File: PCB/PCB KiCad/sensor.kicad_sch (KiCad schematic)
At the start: 15 parts

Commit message: first check + add connectors
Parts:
- removed C? (x2): 100n, symbol Device:C
- removed R?: 100, symbol Device:R
- removed R?: 1k, symbol Device:R
- added C?: 100p, symbol Device:C
- added C?: 47n, symbol Device:C
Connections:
- net AIN+: now also C?.1, C?.2
- net AIN-: now also C?.1, C?.2
- net at R?.1: now also C?.2, R?.2, U?.1
- net at R?.1: now also C?.2, R?.1, U?.7
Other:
- moved on the sheet: R?

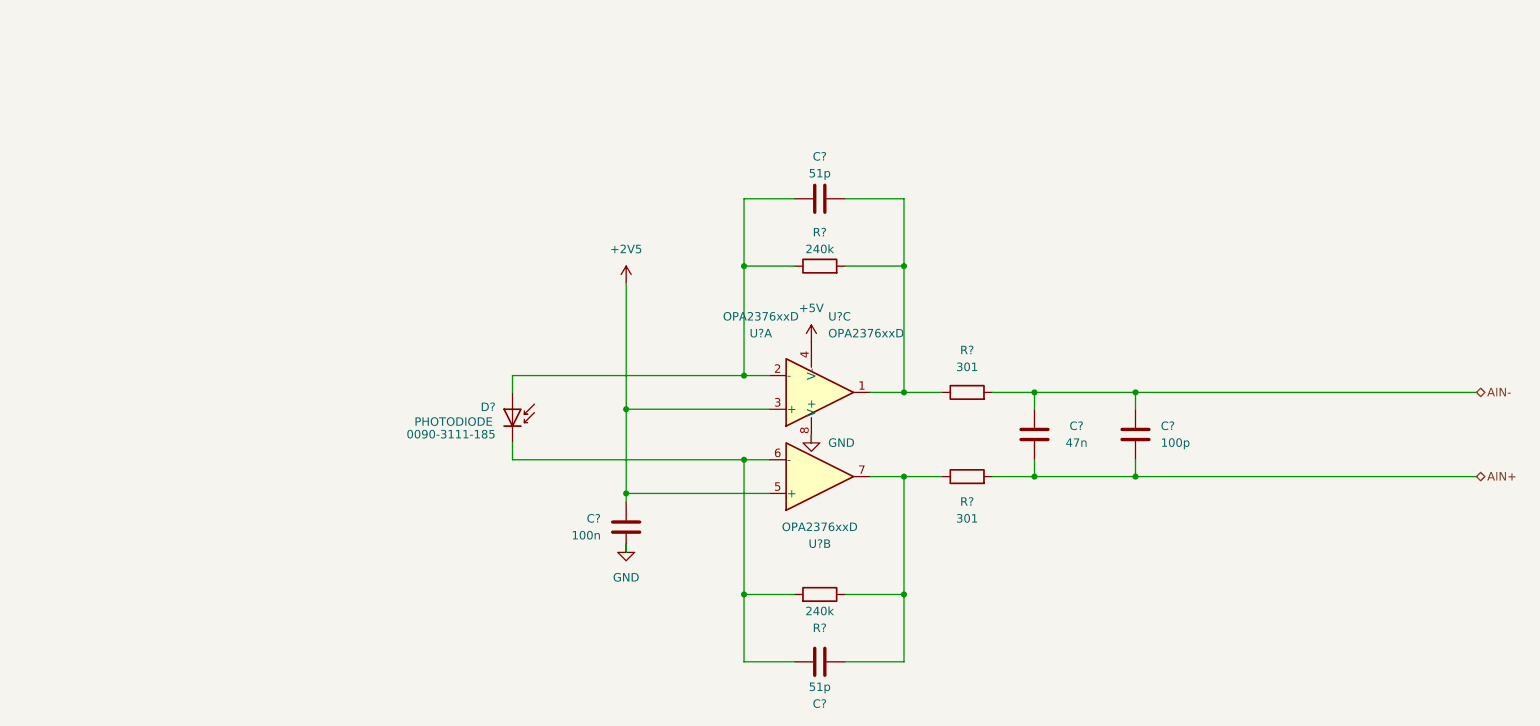
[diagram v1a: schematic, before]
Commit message: ERC: add power flags to satisfy the ERC crap
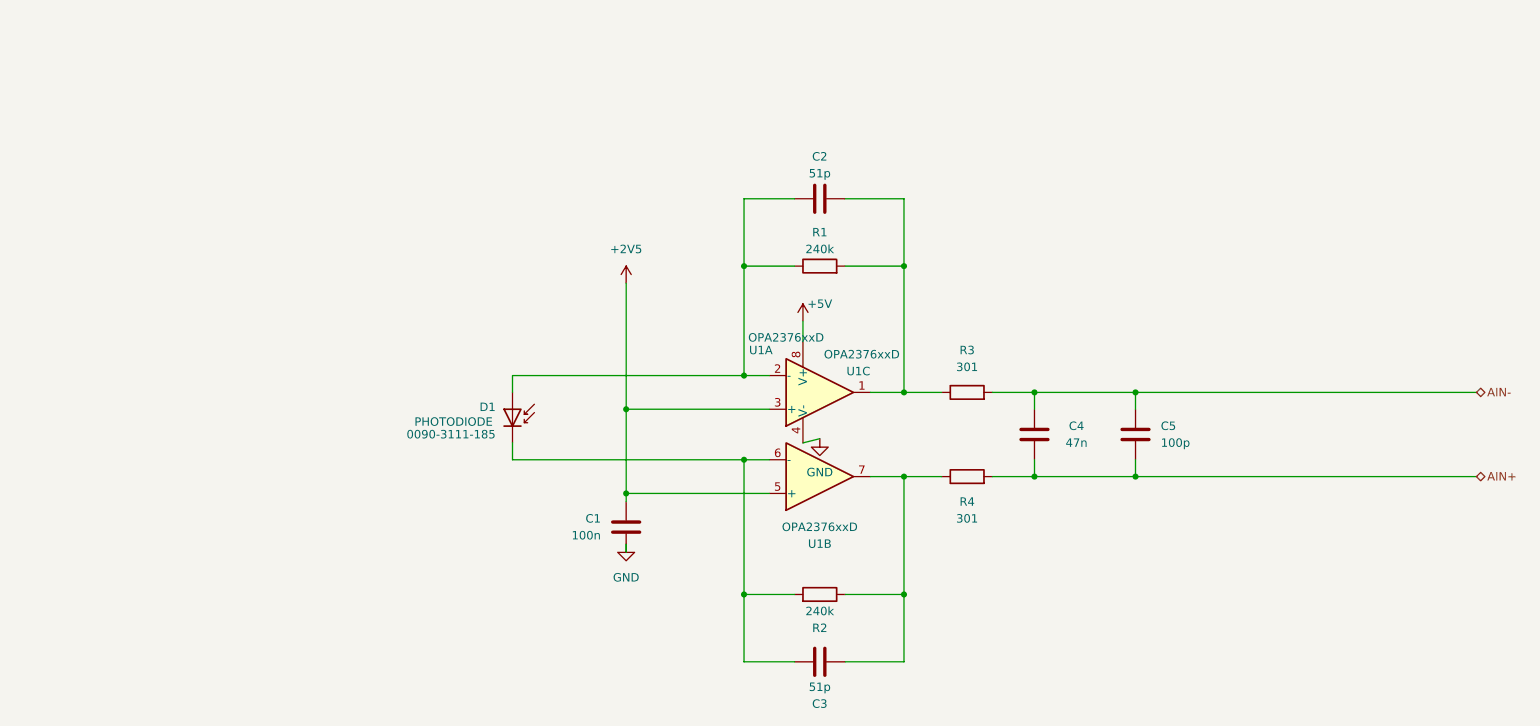
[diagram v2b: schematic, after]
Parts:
- gave numbers to parts that had none: 11
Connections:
- net +5V: now also U1.8 (V+); no longer U1.4 (V-)
- net GND: now also U1.4 (V-); no longer U1.8 (V+)
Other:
- moved on the sheet: U1C
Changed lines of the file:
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@@
     (stroke (width 0) (type default) (color 0 0 0 0))
   )
-  (wire (pts (xy 130.175 99.06) (xy 130.175 100.33))
+  (wire (pts (xy 128.905 100.33) (xy 131.445 99.695))
+    (stroke (width 0) (type default) (color 0 0 0 0))
+  )
+  (wire (pts (xy 128.905 81.915) (xy 128.905 85.09))
     (stroke (width 0) (type default) (color 0 0 0 0))
   )
@@
   (symbol (lib_id "power:GND") (at 102.235 115.57 0) (unit 1)
     (in_bom yes) (on_board yes) (fields_autoplaced)
-    (property "Reference" "#PWR?" (id 0) (at 102.235 121.92 0)
+    (property "Reference" "#PWR02" (id 0) (at 102.235 121.92 0)
       (effects (font (size 1.27 1.27)) hide)
     )
@@
   (symbol (lib_id "Device:R") (at 131.445 123.19 270) (mirror x) (unit 1)
     (in_bom yes) (on_board yes)
-    (property "Reference" "R?" (id 0) (at 131.445 128.27 90))
+    (property "Reference" "R2" (id 0) (at 131.445 128.27 90))
     (property "Value" "240k" (id 1) (at 131.445 125.73 90))
     (property "Footprint" "" (id 2) (at 131.445 124.968 90)
@@
   (symbol (lib_id "Device:R") (at 153.67 92.71 90) (unit 1)
     (in_bom yes) (on_board yes)
-    (property "Reference" "R?" (id 0) (at 153.67 86.36 90))
+    (property "Reference" "R3" (id 0) (at 153.67 86.36 90))
     (property "Value" "301" (id 1) (at 153.67 88.9 90))
     (property "Footprint" "" (id 2) (at 153.67 94.488 90)
@@
   (symbol (lib_id "Device:R") (at 131.445 73.66 90) (unit 1)
     (in_bom yes) (on_board yes)
-    (property "Reference" "R?" (id 0) (at 131.445 68.58 90))
+    (property "Reference" "R1" (id 0) (at 131.445 68.58 90))
     (property "Value" "240k" (id 1) (at 131.445 71.12 90))
     (property "Footprint" "" (id 2) (at 131.445 75.438 90)
@@
   (symbol (lib_id "Device:C") (at 179.07 99.06 0) (unit 1)
     (in_bom yes) (on_board yes) (fields_autoplaced)
-    (property "Reference" "C?" (id 0) (at 182.88 97.7899 0)
+    (property "Reference" "C5" (id 0) (at 182.88 97.7899 0)
       (effects (font (size 1.27 1.27)) (justify left))
     )
@@
     (pin "2")
   )
-  (symbol (lib_id "power:+5V") (at 130.175 85.09 0) (unit 1)
-    (in_bom yes) (on_board yes) (fields_autoplaced)
-    (property "Reference" "#PWR?" (id 0) (at 130.175 88.9 0)
-      (effects (font (size 1.27 1.27)) hide)
-    )
-    (property "Value" "+5V" (id 1) (at 130.175 80.01 0))
-    (property "Footprint" "" (id 2) (at 130.175 85.09 0)
-      (effects (font (size 1.27 1.27)) hide)
-    )
-    (property "Datasheet" "" (id 3) (at 130.175 85.09 0)
+  (symbol (lib_id "power:+5V") (at 128.905 81.915 0) (unit 1)
+    (in_bom yes) (on_board yes)
+    (property "Reference" "#PWR03" (id 0) (at 128.905 85.725 0)
+      (effects (font (size 1.27 1.27)) hide)
+    )
+    (property "Value" "+5V" (id 1) (at 131.445 79.375 0))
+    (property "Footprint" "" (id 2) (at 128.905 81.915 0)
+      (effects (font (size 1.27 1.27)) hide)
+    )
+    (property "Datasheet" "" (id 3) (at 128.905 81.915 0)
       (effects (font (size 1.27 1.27)) hide)
     )
@@
   (symbol (lib_id "power:+2V5") (at 102.235 76.2 0) (unit 1)
     (in_bom yes) (on_board yes) (fields_autoplaced)
-    (property "Reference" "#PWR?" (id 0) (at 102.235 80.01 0)
+    (property "Reference" "#PWR01" (id 0) (at 102.235 80.01 0)
       (effects (font (size 1.27 1.27)) hide)
     )
@@
     (pin "1")
   )
-  (symbol (lib_id "Amplifier_Operational:OPA2376xxD") (at 127.635 92.71 180) (unit 3)
-    (in_bom yes) (on_board yes)
-    (property "Reference" "U?" (id 0) (at 132.715 81.28 0)
-      (effects (font (size 1.27 1.27)) (justify right))
-    )
-    (property "Value" "OPA2376xxD" (id 1) (at 132.715 83.82 0)
-      (effects (font (size 1.27 1.27)) (justify right))
-    )
-    (property "Footprint" "" (id 2) (at 127.635 92.71 0)
-      (effects (font (size 1.27 1.27)) hide)
-    )
-    (property "Datasheet" "http://www.ti.com/lit/ds/symlink/opa376.pdf" (id 3) (at 127.635 92.71 0)
+  (symbol (lib_id "Amplifier_Operational:OPA2376xxD") (at 131.445 92.71 0) (unit 3)
+    (in_bom yes) (on_board yes)
+    (property "Reference" "U1" (id 0) (at 139.065 89.535 0)
+      (effects (font (size 1.27 1.27)) (justify right))
+    )
+    (property "Value" "OPA2376xxD" (id 1) (at 143.51 86.995 0)
+      (effects (font (size 1.27 1.27)) (justify right))
+    )
+    (property "Footprint" "" (id 2) (at 131.445 92.71 0)
+      (effects (font (size 1.27 1.27)) hide)
+    )
+    (property "Datasheet" "http://www.ti.com/lit/ds/symlink/opa376.pdf" (id 3) (at 131.445 92.71 0)
       (effects (font (size 1.27 1.27)) hide)
     )
@@
   (symbol (lib_id "Device:C") (at 131.445 133.35 90) (unit 1)
     (in_bom yes) (on_board yes)
-    (property "Reference" "C?" (id 0) (at 131.445 139.7 90))
+    (property "Reference" "C3" (id 0) (at 131.445 139.7 90))
     (property "Value" "51p" (id 1) (at 131.445 137.16 90))
     (property "Footprint" "" (id 2) (at 135.255 132.3848 0)
@@
     (pin "2")
   )
+  (symbol (lib_id "power:GND") (at 131.445 99.695 0) (unit 1)
+    (in_bom yes) (on_board yes) (fields_autoplaced)
+    (property "Reference" "#PWR04" (id 0) (at 131.445 106.045 0)
+      (effects (font (size 1.27 1.27)) hide)
+    )
+    (property "Value" "GND" (id 1) (at 131.445 104.775 0))
+    (property "Footprint" "" (id 2) (at 131.445 99.695 0)
+      (effects (font (size 1.27 1.27)) hide)
+    )
+    (property "Datasheet" "" (id 3) (at 131.445 99.695 0)
+      (effects (font (size 1.27 1.27)) hide)
+    )
+    (pin "1")
+  )
   (symbol (lib_id "Amplifier_Operational:OPA2376xxD") (at 131.445 92.71 0) (mirror x) (unit 1)
     (in_bom yes) (on_board yes)
-    (property "Reference" "U?" (id 0) (at 122.555 83.82 0))
-    (property "Value" "OPA2376xxD" (id 1) (at 122.555 81.28 0))
+    (property "Reference" "U1" (id 0) (at 122.555 86.36 0))
+    (property "Value" "OPA2376xxD" (id 1) (at 126.365 84.455 0))
     (property "Footprint" "" (id 2) (at 131.445 92.71 0)
       (effects (font (size 1.27 1.27)) hide)
@@
     (pin "3")
   )
-  (symbol (lib_id "power:GND") (at 130.175 99.06 0) (unit 1)
-    (in_bom yes) (on_board yes) (fields_autoplaced)
-    (property "Reference" "#PWR?" (id 0) (at 130.175 105.41 0)
-      (effects (font (size 1.27 1.27)) hide)
-    )
-    (property "Value" "GND" (id 1) (at 132.715 100.3299 0)
-      (effects (font (size 1.27 1.27)) (justify left))
-    )
-    (property "Footprint" "" (id 2) (at 130.175 99.06 0)
-      (effects (font (size 1.27 1.27)) hide)
-    )
-    (property "Datasheet" "" (id 3) (at 130.175 99.06 0)
-      (effects (font (size 1.27 1.27)) hide)
-    )
-    (pin "1")
-  )
   (symbol (lib_id "Device:C") (at 131.445 63.5 90) (unit 1)
     (in_bom yes) (on_board yes)
-    (property "Reference" "C?" (id 0) (at 131.445 57.15 90))
+    (property "Reference" "C2" (id 0) (at 131.445 57.15 90))
     (property "Value" "51p" (id 1) (at 131.445 59.69 90))
     (property "Footprint" "" (id 2) (at 135.255 62.5348 0)
@@
   (symbol (lib_id "Device:C") (at 163.83 99.06 180) (unit 1)
     (in_bom yes) (on_board yes)
-    (property "Reference" "C?" (id 0) (at 170.18 97.79 0))
+    (property "Reference" "C4" (id 0) (at 170.18 97.79 0))
     (property "Value" "47n" (id 1) (at 170.18 100.33 0))
     (property "Footprint" "" (id 2) (at 162.8648 95.25 0)
@@
   (symbol (lib_id "Device:R") (at 153.67 105.41 90) (unit 1)
     (in_bom yes) (on_board yes)
-    (property "Reference" "R?" (id 0) (at 153.67 109.22 90))
+    (property "Reference" "R4" (id 0) (at 153.67 109.22 90))
     (property "Value" "301" (id 1) (at 153.67 111.76 90))
     (property "Footprint" "" (id 2) (at 153.67 107.188 90)
@@
   (symbol (lib_id "Amplifier_Operational:OPA2376xxD") (at 131.445 105.41 0) (mirror x) (unit 2)
     (in_bom yes) (on_board yes)
-    (property "Reference" "U?" (id 0) (at 131.445 115.57 0))
+    (property "Reference" "U1" (id 0) (at 131.445 115.57 0))
     (property "Value" "OPA2376xxD" (id 1) (at 131.445 113.03 0))
     (property "Footprint" "" (id 2) (at 131.445 105.41 0)
@@
   (symbol (lib_id "Device:D_Photo") (at 85.09 95.25 270) (mirror x) (unit 1)
     (in_bom yes) (on_board yes)
-    (property "Reference" "D?" (id 0) (at 82.55 94.9324 90)
+    (property "Reference" "D1" (id 0) (at 82.55 94.9324 90)
       (effects (font (size 1.27 1.27)) (justify right))
     )
@@
   (symbol (lib_id "Device:C") (at 102.235 113.03 0) (mirror x) (unit 1)
     (in_bom yes) (on_board yes) (fields_autoplaced)
-    (property "Reference" "C?" (id 0) (at 98.425 111.7599 0)
-      (effects (font (size 1.27 1.27)) (justify right))
-    )
+    (property "Reference" "C1" (id 0) (at 98.425 111.7599 0)
+      (effects (font (size 1.27 1.27)) (justify right))
+    )

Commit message: Add footprints
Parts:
- C1, C2, C3, C4, C5: footprint (none) -> Capacitor_SMD:C_0805_2012Metric_Pad1.18x1.45mm_HandSolder
- D1: footprint (none) -> Diode_SMD:D_1206_3216Metric_Pad1.42x1.75mm_HandSolder
- R1, R2, R3, R4: footprint (none) -> Resistor_SMD:R_0805_2012Metric_Pad1.20x1.40mm_HandSolder
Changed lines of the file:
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@@
     (property "Reference" "R2" (id 0) (at 131.445 128.27 90))
     (property "Value" "240k" (id 1) (at 131.445 125.73 90))
-    (property "Footprint" "" (id 2) (at 131.445 124.968 90)
+    (property "Footprint" "Resistor_SMD:R_0805_2012Metric_Pad1.20x1.40mm_HandSolder" (id 2) (at 131.445 124.968 90)
       (effects (font (size 1.27 1.27)) hide)
     )
@@
     (property "Reference" "R3" (id 0) (at 153.67 86.36 90))
     (property "Value" "301" (id 1) (at 153.67 88.9 90))
-    (property "Footprint" "" (id 2) (at 153.67 94.488 90)
+    (property "Footprint" "Resistor_SMD:R_0805_2012Metric_Pad1.20x1.40mm_HandSolder" (id 2) (at 153.67 94.488 90)
       (effects (font (size 1.27 1.27)) hide)
     )
@@
     (property "Reference" "R1" (id 0) (at 131.445 68.58 90))
     (property "Value" "240k" (id 1) (at 131.445 71.12 90))
-    (property "Footprint" "" (id 2) (at 131.445 75.438 90)
+    (property "Footprint" "Resistor_SMD:R_0805_2012Metric_Pad1.20x1.40mm_HandSolder" (id 2) (at 131.445 75.438 90)
       (effects (font (size 1.27 1.27)) hide)
     )
@@
       (effects (font (size 1.27 1.27)) (justify left))
     )
-    (property "Footprint" "" (id 2) (at 180.0352 102.87 0)
+    (property "Footprint" "Capacitor_SMD:C_0805_2012Metric_Pad1.18x1.45mm_HandSolder" (id 2) (at 180.0352 102.87 0)
       (effects (font (size 1.27 1.27)) hide)
     )
@@
     (property "Reference" "C3" (id 0) (at 131.445 139.7 90))
     (property "Value" "51p" (id 1) (at 131.445 137.16 90))
-    (property "Footprint" "" (id 2) (at 135.255 132.3848 0)
+    (property "Footprint" "Capacitor_SMD:C_0805_2012Metric_Pad1.18x1.45mm_HandSolder" (id 2) (at 135.255 132.3848 0)
       (effects (font (size 1.27 1.27)) hide)
     )
@@
     (property "Reference" "C2" (id 0) (at 131.445 57.15 90))
     (property "Value" "51p" (id 1) (at 131.445 59.69 90))
-    (property "Footprint" "" (id 2) (at 135.255 62.5348 0)
+    (property "Footprint" "Capacitor_SMD:C_0805_2012Metric_Pad1.18x1.45mm_HandSolder" (id 2) (at 135.255 62.5348 0)
       (effects (font (size 1.27 1.27)) hide)
     )
@@
     (property "Reference" "C4" (id 0) (at 170.18 97.79 0))
     (property "Value" "47n" (id 1) (at 170.18 100.33 0))
-    (property "Footprint" "" (id 2) (at 162.8648 95.25 0)
+    (property "Footprint" "Capacitor_SMD:C_0805_2012Metric_Pad1.18x1.45mm_HandSolder" (id 2) (at 162.8648 95.25 0)
       (effects (font (size 1.27 1.27)) hide)
     )
@@
     (property "Reference" "R4" (id 0) (at 153.67 109.22 90))
     (property "Value" "301" (id 1) (at 153.67 111.76 90))
-    (property "Footprint" "" (id 2) (at 153.67 107.188 90)
+    (property "Footprint" "Resistor_SMD:R_0805_2012Metric_Pad1.20x1.40mm_HandSolder" (id 2) (at 153.67 107.188 90)
       (effects (font (size 1.27 1.27)) hide)
     )
@@
       (effects (font (size 1.27 1.27)) (justify right))
     )
-    (property "Footprint" "" (id 2) (at 85.09 96.52 0)
+    (property "Footprint" "Diode_SMD:D_1206_3216Metric_Pad1.42x1.75mm_HandSolder" (id 2) (at 85.09 96.52 0)
       (effects (font (size 1.27 1.27)) hide)
     )
@@
       (effects (font (size 1.27 1.27)) (justify right))
     )
-    (property "Footprint" "" (id 2) (at 103.2002 109.22 0)
-      (effects (font (size 1.27 1.27)) hide)
-    )
+    (property "Footprint" "Capacitor_SMD:C_0805_2012Metric_Pad1.18x1.45mm_HandSolder" (id 2) (at 103.2002 109.22 0)
+      (effects (font (size 1.27 1.27)) hide)
+    )

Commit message: Added missing footprint symbols
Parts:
- U1: footprint (none) -> eec:Texas_Instruments-OPA2376AID-Level_A
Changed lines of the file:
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@@
       (effects (font (size 1.27 1.27)) (justify right))
     )
-    (property "Footprint" "" (id 2) (at 131.445 92.71 0)
+    (property "Footprint" "eec:Texas_Instruments-OPA2376AID-Level_A" (id 2) (at 131.445 92.71 0)
       (effects (font (size 1.27 1.27)) hide)
     )
@@
     (property "Reference" "U1" (id 0) (at 122.555 86.36 0))
     (property "Value" "OPA2376xxD" (id 1) (at 126.365 84.455 0))
-    (property "Footprint" "" (id 2) (at 131.445 92.71 0)
+    (property "Footprint" "eec:Texas_Instruments-OPA2376AID-Level_A" (id 2) (at 131.445 92.71 0)
       (effects (font (size 1.27 1.27)) hide)
     )
@@
     (property "Reference" "U1" (id 0) (at 131.445 115.57 0))
     (property "Value" "OPA2376xxD" (id 1) (at 131.445 113.03 0))
-    (property "Footprint" "" (id 2) (at 131.445 105.41 0)
+    (property "Footprint" "eec:Texas_Instruments-OPA2376AID-Level_A" (id 2) (at 131.445 105.41 0)
       (effects (font (size 1.27 1.27)) hide)
     )

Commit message: export for review
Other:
- company: (none) -> Plastic Scanner
- title: (none) -> Development Board
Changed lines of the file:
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@@
 (kicad_sch (version 20211123) (generator eeschema)
   (paper "A4")
+  (title_block
+    (title "Development Board")
+    (date "2022-03-15")
+    (rev "2.1")
+    (company "Plastic Scanner")
+  )
   (junction (at 144.145 92.71) (diameter 0) (color 0 0 0 0)
   )

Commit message: PCB at time of order
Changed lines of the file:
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@@
   (symbol (lib_id "Amplifier_Operational:OPA2376xxD") (at 131.445 92.71 0) (unit 3)
     (in_bom yes) (on_board yes)
-    (property "Reference" "U1" (id 0) (at 139.065 89.535 0)
+    (property "Reference" "U1" (id 0) (at 138.43 100.33 0)
       (effects (font (size 1.27 1.27)) (justify right))
     )
-    (property "Value" "OPA2376xxD" (id 1) (at 143.51 86.995 0)
+    (property "Value" "OPA2376xxD" (id 1) (at 146.05 97.79 0)
       (effects (font (size 1.27 1.27)) (justify right))
     )
@@
   (symbol (lib_id "Amplifier_Operational:OPA2376xxD") (at 131.445 92.71 0) (mirror x) (unit 1)
     (in_bom yes) (on_board yes)
-    (property "Reference" "U1" (id 0) (at 122.555 86.36 0))
-    (property "Value" "OPA2376xxD" (id 1) (at 126.365 84.455 0))
+    (property "Reference" "U1" (id 0) (at 133.35 87.63 0))
+    (property "Value" "OPA2376xxD" (id 1) (at 137.16 85.09 0))
     (property "Footprint" "eec:Texas_Instruments-OPA2376AID-Level_A" (id 2) (at 131.445 92.71 0)
       (effects (font (size 1.27 1.27)) hide)
